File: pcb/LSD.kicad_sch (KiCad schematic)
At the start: 7 parts, among them Q1 STS5DNF60L

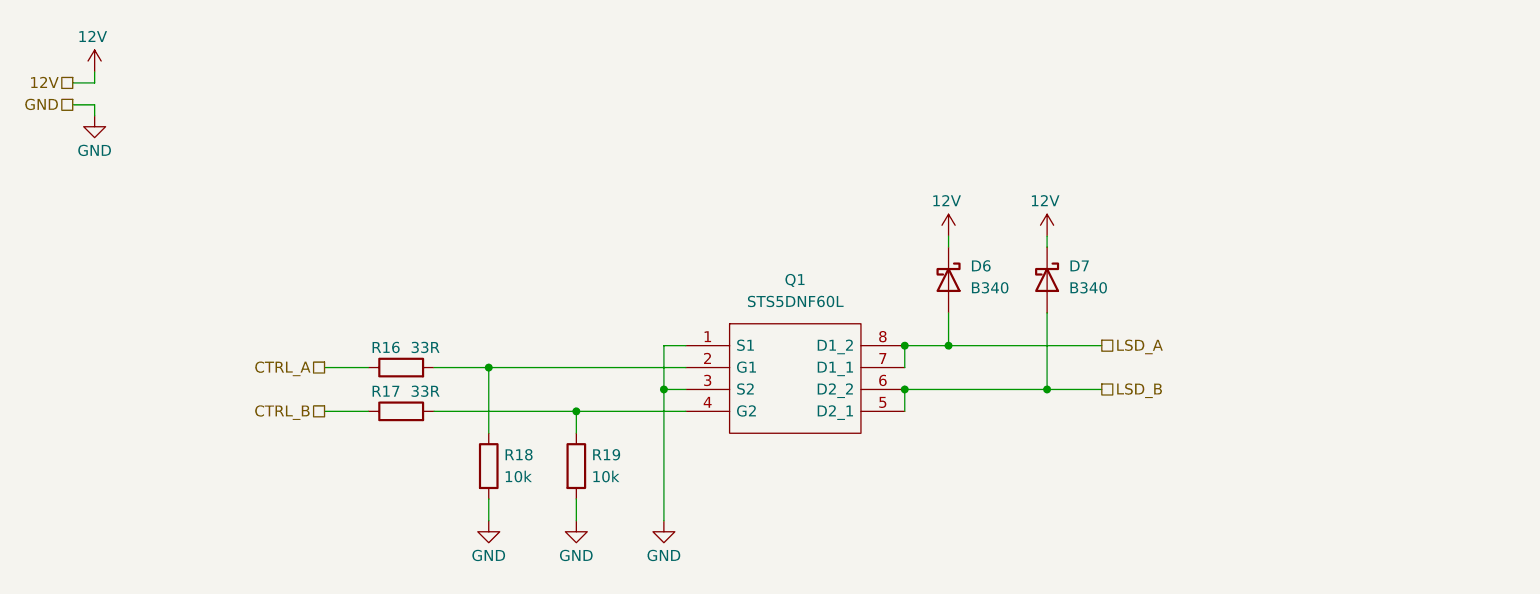
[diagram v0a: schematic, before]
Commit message: added better lsds
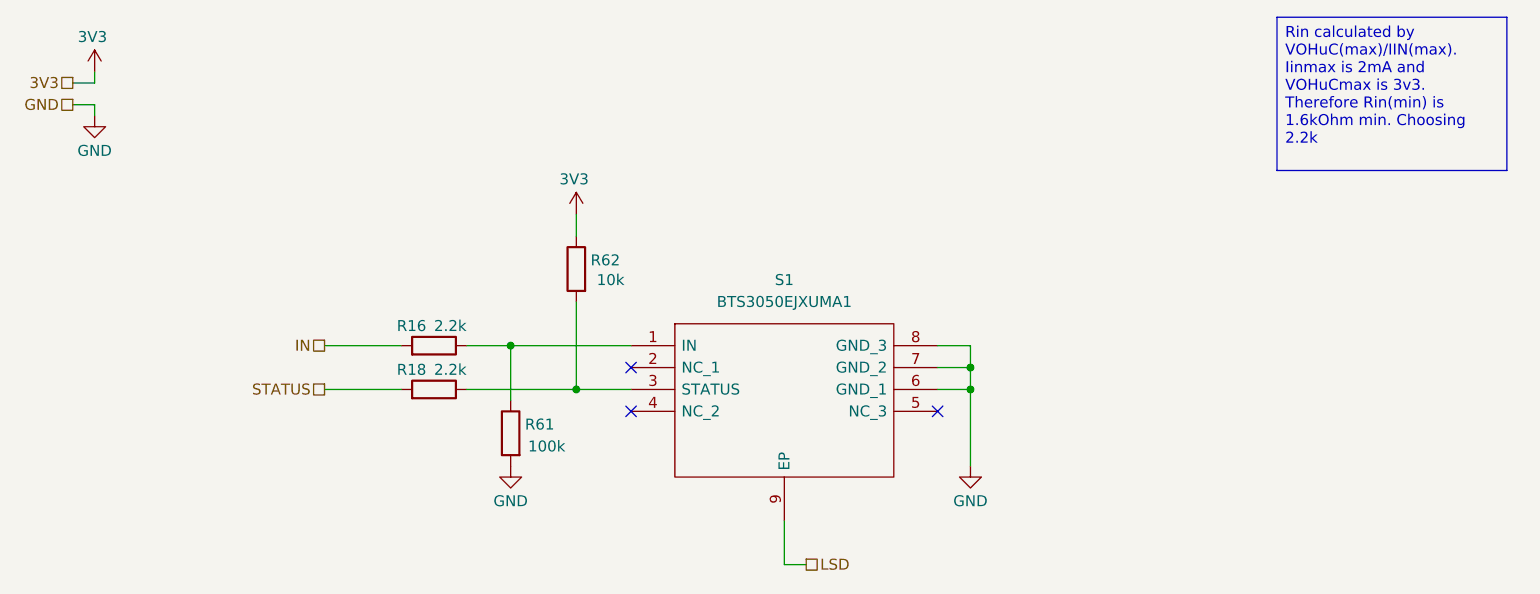
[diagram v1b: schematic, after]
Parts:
- removed D6, D7: B340, Diode_SMD:D_SMC, symbol Diode:B340
- removed Q1: STS5DNF60L, SOIC127P600X175-8N, symbol 0_SamacSys_Parts:STS5DNF60L
- removed R17: 33R, Resistor_SMD:R_0603_1608Metric_Pad0.98x0.95mm_HandSolder, symbol Device:R
- removed R19: 10k, Resistor_SMD:R_0603_1608Metric_Pad0.98x0.95mm_HandSolder, symbol Device:R
- added R61: 100k, Resistor_SMD:R_0603_1608Metric_Pad0.98x0.95mm_HandSolder, symbol Device:R
- added R62: 10k, Resistor_SMD:R_0603_1608Metric_Pad0.98x0.95mm_HandSolder, symbol Device:R
- added S1: BTS3050EJXUMA1, SOIC127P600X115-9N, symbol 0_SamacSys_Parts:BTS3050EJXUMA1
- R16: value 33R -> 2.2k
- R18: value 10k -> 2.2k
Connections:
- net GND: now also R61.2, S1.6 (GND_1), S1.7 (GND_2), S1.8 (GND_3); no longer R18.2
- net at R18.1: now also R62.2, S1.3 (STATUS); no longer R16.2
- net CTRL_A: no longer names the net of R16.1
- net CTRL_A: now also R61.1, S1.1 (IN)
- new net 3V3: R62.1
- new net IN: R16.2
- new net LSD: S1.9 (EP)
- new net STATUS: R18.2
- no-connect marks 0 -> 3

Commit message: added USB protection, reviewed LSD and HSD, improved input TVS footprint
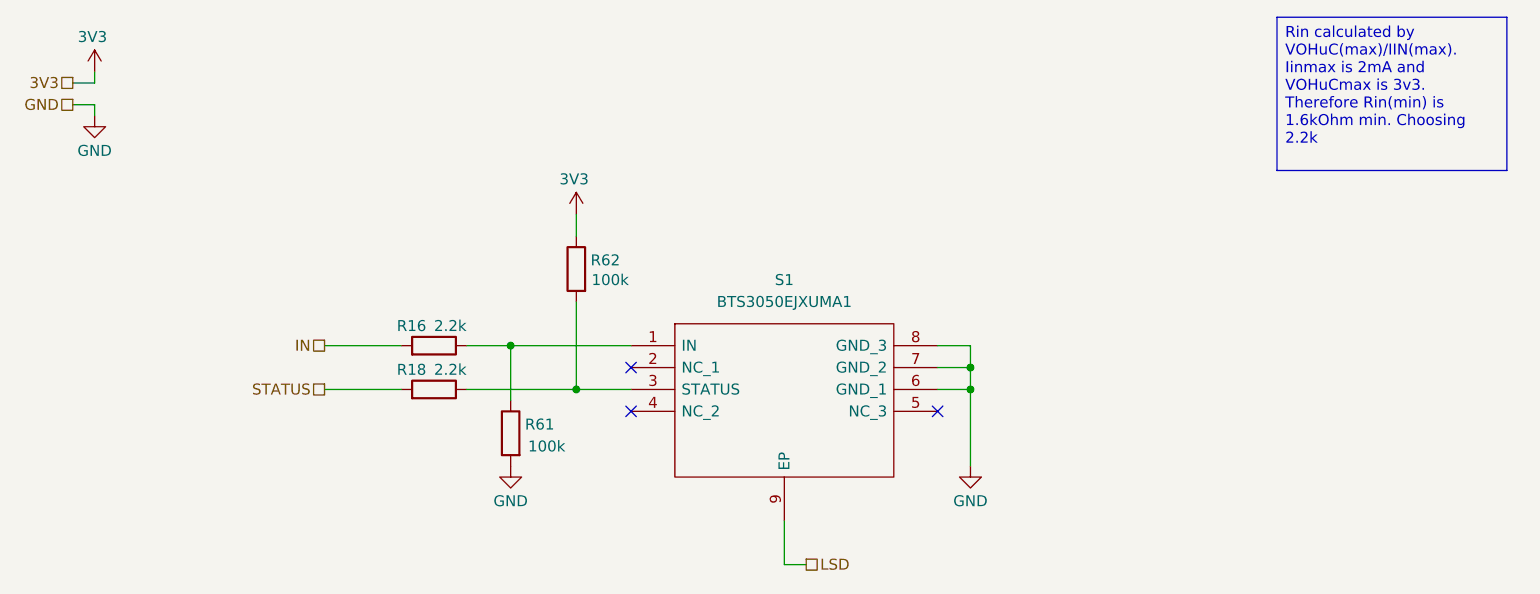
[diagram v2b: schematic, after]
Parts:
- R62: value 10k -> 100k
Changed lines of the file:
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@@
 			)
 		)
-		(property "Value" "10k"
-			(at 89.408 45.72 0)
+		(property "Value" "100k"
+			(at 89.916 45.72 0)
 			(effects
 				(font

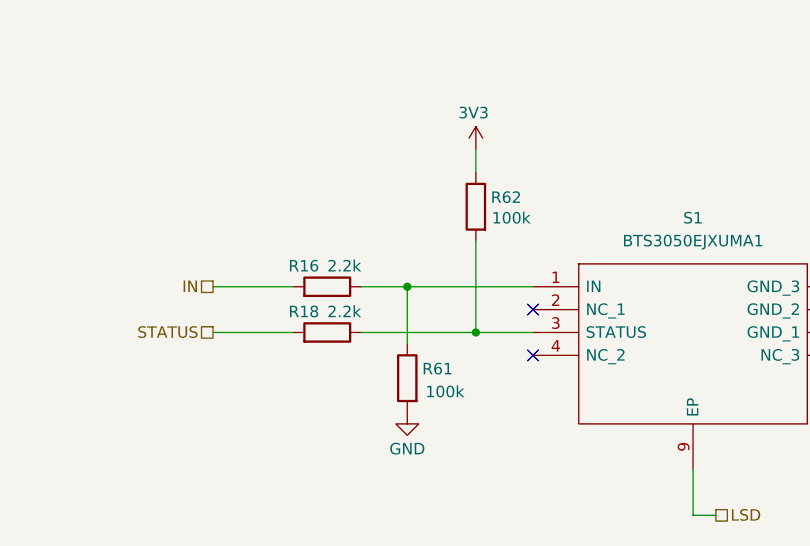
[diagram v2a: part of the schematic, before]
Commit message: reannotated, updated some symbols
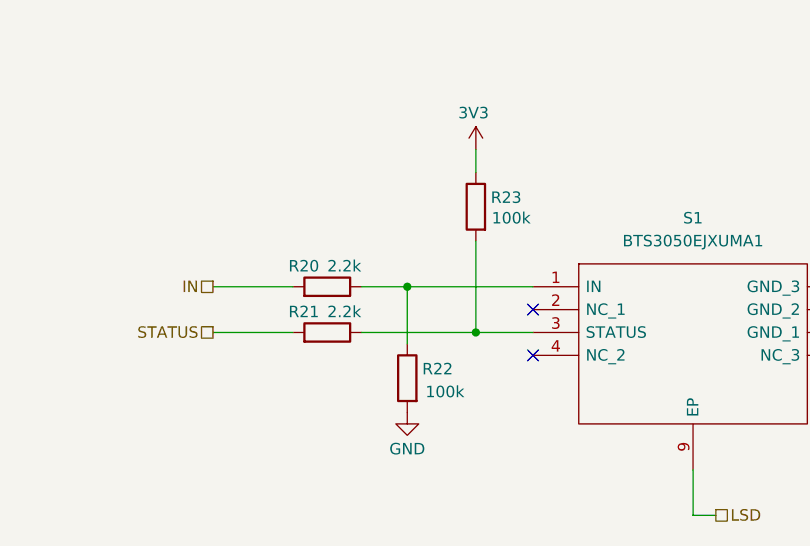
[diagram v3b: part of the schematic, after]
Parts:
- renumbered R16 to R20, R18 to R21, R61 to R22, R62 to R23
